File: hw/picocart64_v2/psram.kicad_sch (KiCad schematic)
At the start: 20 parts, among them U1 LY68L6400SLIT, U2 LY68L6400SLIT, U3 LY68L6400SLIT, U4 LY68L6400SLIT, U5 LY68L6400SLIT, U6 LY68L6400SLIT, U7 LY68L6400SLIT, U8 LY68L6400SLIT, U9 SN74LVC138AQDRQ1

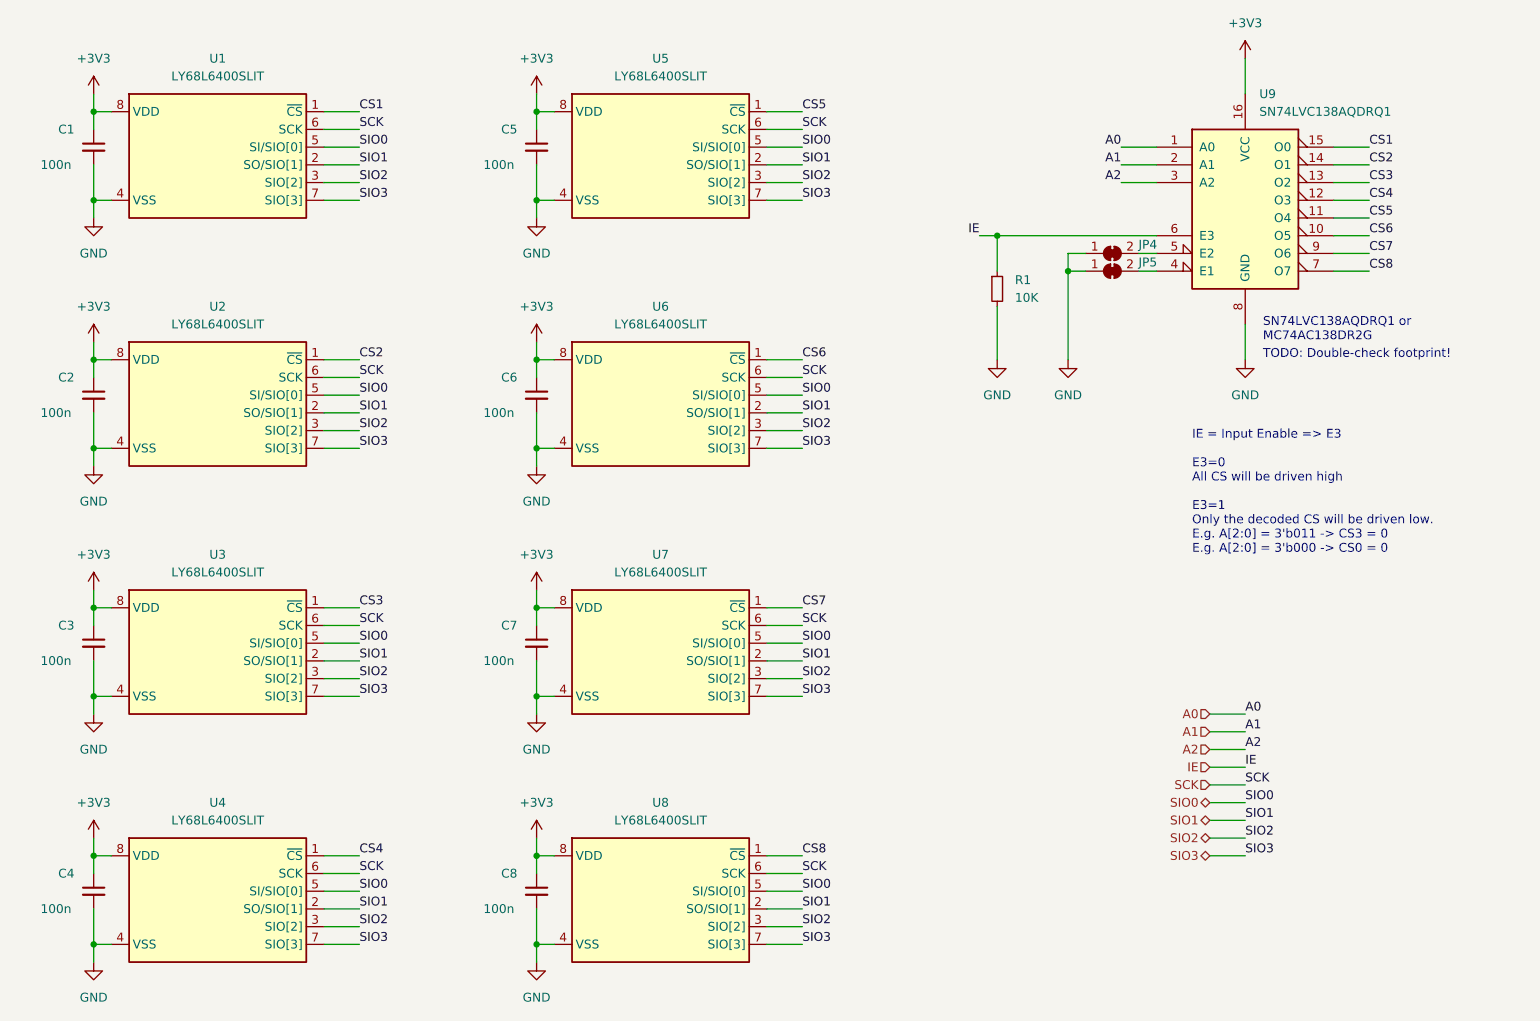
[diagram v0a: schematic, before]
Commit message: Adding flash memory to the psram array kicad page.
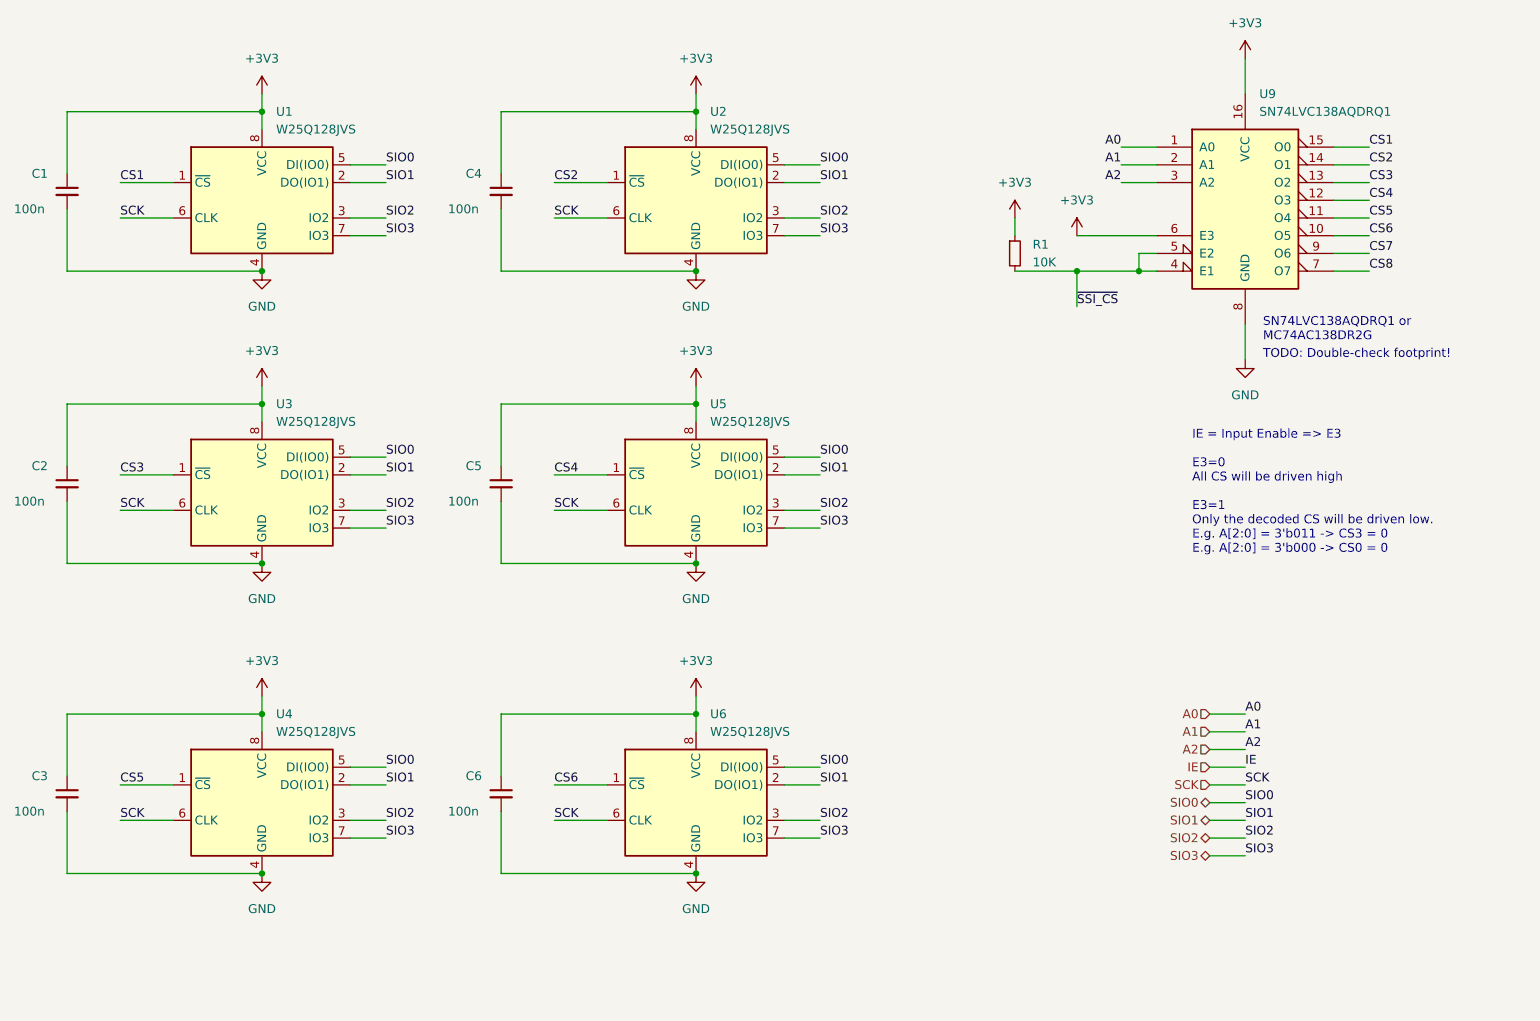
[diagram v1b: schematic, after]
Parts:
- removed C7, C8: 100n, Capacitor_SMD:C_0402_1005Metric, symbol Device:C_Small
- removed JP4, JP5: SolderJumper_2_Bridged, picocart64:SolderJumper-2_Small_Closed, symbol Jumper:SolderJumper_2_Bridged
- removed U1, U2, U3, U4, U5, U6, U7, U8: LY68L6400SLIT, Package_SO:SOIC-8_5.275x5.275mm_P1.27mm, symbol spiram:LY68L6400SLIT
- added U1, U2, U3, U4, U5, U6: W25Q128JVS, Package_SO:SOIC-8_5.23x5.23mm_P1.27mm, symbol Memory_Flash:W25Q128JVS
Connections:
- net +3V3: now also R1.1, U9.6 (E3), U1.8 (VCC), U2.8 (VCC), U3.8 (VCC), U4.8 (VCC), U5.8 (VCC), U6.8 (VCC)
- net CS1: now also U1.1 (~{CS})
- net CS2: now also U2.1 (~{CS})
- net CS3: now also U3.1 (~{CS})
- net CS4: now also U5.1 (~{CS})
- net CS5: now also U4.1 (~{CS})
- net CS6: now also U6.1 (~{CS})
- net GND: now also U1.4 (GND), U2.4 (GND), U3.4 (GND), U4.4 (GND), U5.4 (GND), U6.4 (GND); no longer R1.2
- net IE: no longer R1.1, U9.6 (E3)
- net SCK: now also U1.6 (CLK), U2.6 (CLK), U3.6 (CLK), U4.6 (CLK), U5.6 (CLK), U6.6 (CLK)
- net SIO0: now also U1.5 (DI(IO0)), U2.5 (DI(IO0)), U3.5 (DI(IO0)), U4.5 (DI(IO0)), U5.5 (DI(IO0)), U6.5 (DI(IO0))
- net SIO1: now also U1.2 (DO(IO1)), U2.2 (DO(IO1)), U3.2 (DO(IO1)), U4.2 (DO(IO1)), U5.2 (DO(IO1)), U6.2 (DO(IO1))
- net SIO2: now also U1.3 (IO2), U2.3 (IO2), U3.3 (IO2), U4.3 (IO2), U5.3 (IO2), U6.3 (IO2)
- net SIO3: now also U1.7 (IO3), U2.7 (IO3), U3.7 (IO3), U4.7 (IO3), U5.7 (IO3), U6.7 (IO3)
- net ~{SSI_CS}: now reaches U9.4 (E1)
- net ~{SSI_CS}: now also R1.2, U9.5 (E2)

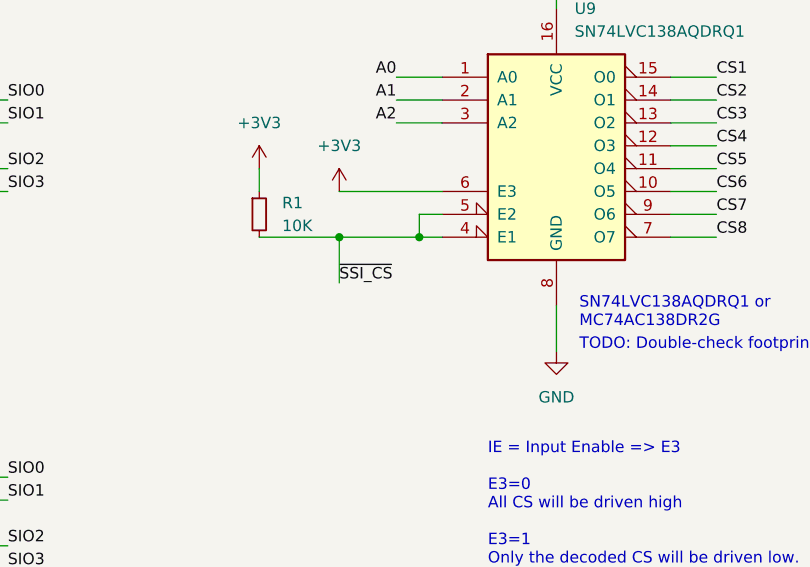
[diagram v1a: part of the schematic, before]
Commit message: Updated schematic for larger resistor arrays, removed the extra flash chip and only use the existing 8 pads, it will default to 1 for booting/loading firmware. Added a reset button to the back. Added company logo and updated text on board.
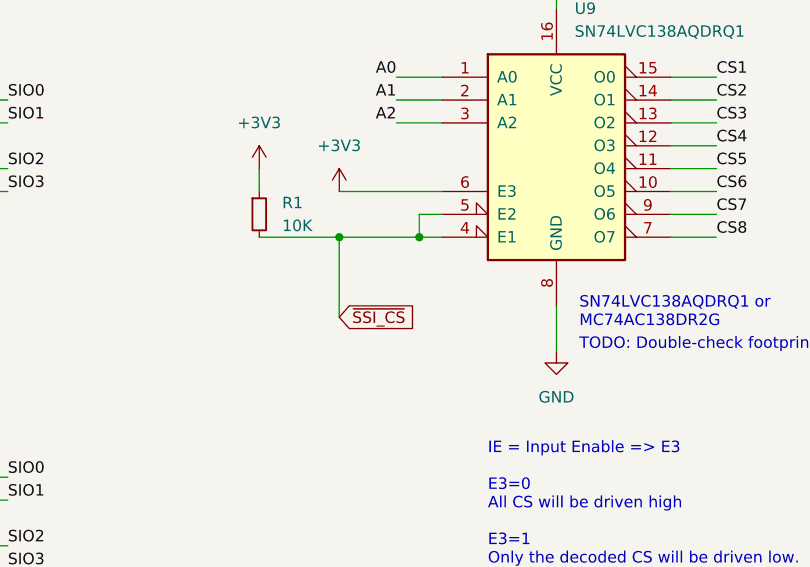
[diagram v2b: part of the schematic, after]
